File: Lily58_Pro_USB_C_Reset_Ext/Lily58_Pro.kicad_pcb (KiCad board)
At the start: 2 copper layers, 7.7 x 45.5 mm, 11 parts, among them J2 4PIN, P1 i2c_pin, P2 i2c_pin, U1 USB4110-GF-A_REVB, U2 USB4110-GF-A_REVB

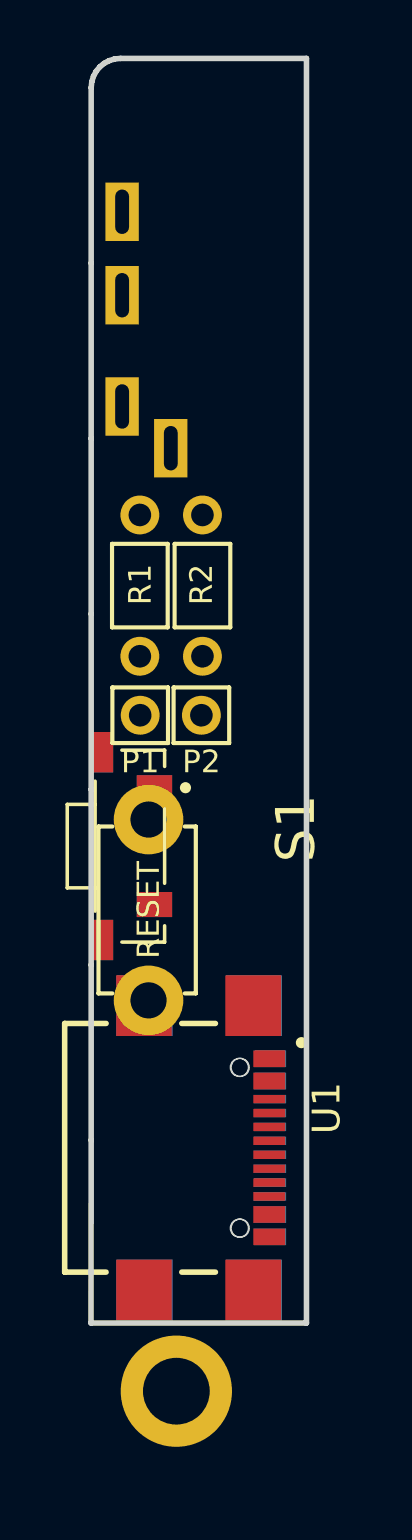
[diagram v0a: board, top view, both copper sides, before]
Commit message: Lily58_Pro_USB_C_Reset_Ext: routing
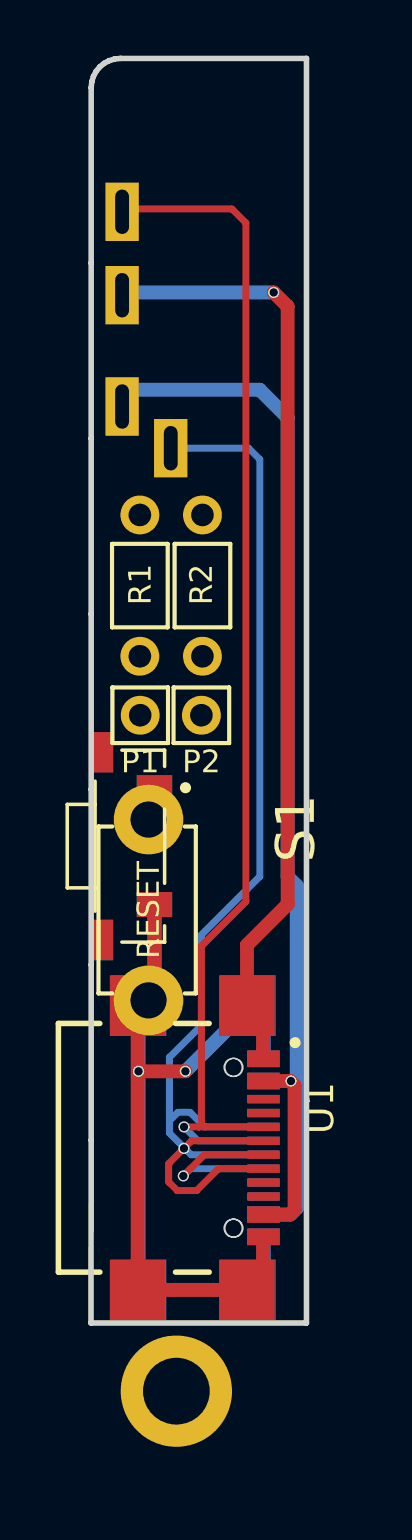
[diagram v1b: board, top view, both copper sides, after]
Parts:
- moved U2 0.23 mm to (88.1, 76.2)
- moved U1 0.22 mm to (88.0, 76.2)
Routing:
- net GND: track 0.00 -> 80.9 mm, vias 0 -> 3
- net SCL: track 0.00 -> 50.0 mm, vias 0 -> 2
- net VCC: track 0.00 -> 44.7 mm, vias 0 -> 1
- net SDA: track 0.00 -> 44.6 mm, vias 0 -> 1
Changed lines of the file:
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@@
   )
   (footprint "Usb:GCT_USB4110-GF-A_REVB" (layer "F.Cu")
-    (at 88.265 76.25 -90)
+    (at 88.04 76.25 -90)
     (property "MANUFACTURER" "GCT")
     (property "MAXIMUM_PACKAGE_HEIGHT" "3.26 mm")
@@
       (effects (font (size 1.4 1.4) (thickness 0.15)))
     )
-    (fp_text value "TL3330AF130QG" (at 9.194 -3.429 -90) (layer "F.Fab")
+    (fp_text value "TL3330AF130QG" (at 9.194 -3.204 -90) (layer "F.Fab")
       (effects (font (size 1.4 1.4) (thickness 0.15)))
     )
@@
   )
   (footprint "Usb:GCT_USB4110-GF-A_REVB" (layer "B.Cu")
-    (at 88.2955 76.25 90)
+    (at 88.0705 76.25 90)
     (property "MANUFACTURER" "GCT")
     (property "MAXIMUM_PACKAGE_HEIGHT" "3.26 mm")
@@
     (style (thickness 0.15) (arrow_length 1.27) (text_position_mode 0) (extension_height 0.58642) (extension_offset 0.5) keep_text_aligned)
   )
+  (segment (start 90.25 78.49) (end 90.09 78.65) (width 0.5) (layer "F.Cu") (net 1))
+  (segment (start 90.09 78.65) (end 89.115 78.65) (width 0.5) (layer "F.Cu") (net 1))
+  (segment (start 90.09 73.85) (end 90.25 74.01) (width 0.5) (layer "F.Cu") (net 1))
+  (segment (start 90.25 74.01) (end 90.25 78.49) (width 0.5) (layer "F.Cu") (net 1))
+  (segment (start 89.115 73.85) (end 90.09 73.85) (width 0.5) (layer "F.Cu") (net 1))
+  (via (at 90.1205 73.85) (size 0.4) (drill 0.3) (layers "F.Cu" "B.Cu") (net 1))
+  (segment (start 90.1 78.65) (end 90.328 78.422) (width 0.5) (layer "B.Cu") (net 1))
+  (segment (start 90.328 78.422) (end 90.328 74.0575) (width 0.5) (layer "B.Cu") (net 1))
+  (segment (start 90 50) (end 89 49) (width 0.5) (layer "B.Cu") (net 1))
+  (segment (start 84.5 49) (end 84.05 49.45) (width 0.5) (layer "B.Cu") (net 1))
+  (segment (start 90.328 74.0575) (end 90.1205 73.85) (width 0.5) (layer "B.Cu") (net 1))
+  (segment (start 89.1455 78.65) (end 90.1 78.65) (width 0.5) (layer "B.Cu") (net 1))
+  (segment (start 84.05 49.45) (end 84.05 49.6) (width 0.5) (layer "B.Cu") (net 1))
+  (segment (start 90 66.5) (end 90 50) (width 0.5) (layer "B.Cu") (net 1))
+  (segment (start 90.328 74.0575) (end 90.328 66.828) (width 0.5) (layer "B.Cu") (net 1))
+  (segment (start 90.328 66.828) (end 90 66.5) (width 0.5) (layer "B.Cu") (net 1))
+  (segment (start 90.1205 73.85) (end 89.1455 73.85) (width 0.5) (layer "B.Cu") (net 1))
+  (segment (start 89 49) (end 84.5 49) (width 0.5) (layer "B.Cu") (net 1))
+  (segment (start 89.115 73.05) (end 89.115 71.715) (width 0.5) (layer "F.Cu") (net 2))
+  (segment (start 85.213 67.505) (end 85.213 70.737) (width 0.5) (layer "F.Cu") (net 2))
+  (segment (start 84.61 71.14) (end 84.61 81.36) (width 0.5) (layer "F.Cu") (net 2))
+  (segment (start 89.115 80.785) (end 88.54 81.36) (width 0.5) (layer "F.Cu") (net 2))
+  (segment (start 88.54 71.14) (end 88.54 68.96) (width 0.5) (layer "F.Cu") (net 2))
+  (segment (start 84.61 81.36) (end 88.54 81.36) (width 0.5) (layer "F.Cu") (net 2))
+  (segment (start 89.115 79.45) (end 89.115 80.785) (width 0.5) (layer "F.Cu") (net 2))
+  (segment (start 84.6405 73.5) (end 86.325 73.5) (width 0.5) (layer "F.Cu") (net 2))
+  (segment (start 89.115 71.715) (end 88.54 71.14) (width 0.5) (layer "F.Cu") (net 2))
+  (segment (start 88.54 68.96) (end 90 67.5) (width 0.5) (layer "F.Cu") (net 2))
+  (segment (start 85.213 70.737) (end 85 70.95) (width 0.5) (layer "F.Cu") (net 2))
+  (segment (start 90 67.5) (end 90 46) (width 0.5) (layer "F.Cu") (net 2))
+  (segment (start 90 46) (end 89.5 45.5) (width 0.5) (layer "F.Cu") (net 2))
+  (via (at 84.6405 73.5) (size 0.4) (drill 0.3) (layers "F.Cu" "B.Cu") (net 2))
+  (via (at 86.325 73.5) (size 0.4) (drill 0.3) (layers "F.Cu" "B.Cu") (net 2))
+  (via (at 89.5 45.5) (size 0.4) (drill 0.3) (layers "F.Cu" "B.Cu") (net 2))
+  (segment (start 84.6405 81.36) (end 84.6405 71.14) (width 0.5) (layer "B.Cu") (net 2))
+  (segment (start 85.213 67.505) (end 85.213 70.737) (width 0.5) (layer "B.Cu") (net 2))
+  (segment (start 89.1455 71.715) (end 88.5705 71.14) (width 0.5) (layer "B.Cu") (net 2))
+  (segment (start 88.5705 71.2545) (end 86.325 73.5) (width 0.5) (layer "B.Cu") (net 2))
+  (segment (start 84.6405 81.36) (end 88.5705 81.36) (width 0.5) (layer "B.Cu") (net 2))
+  (segment (start 84.15 45.5) (end 84.05 45.6) (width 0.5) (layer "B.Cu") (net 2))
+  (segment (start 89.1455 79.45) (end 89.1455 80.785) (width 0.5) (layer "B.Cu") (net 2))
+  (segment (start 89.1455 80.785) (end 88.5705 81.36) (width 0.5) (layer "B.Cu") (net 2))
+  (segment (start 89.5 45.5) (end 84.15 45.5) (width 0.5) (layer "B.Cu") (net 2))
+  (segment (start 85.213 70.737) (end 85 70.95) (width 0.5) (layer "B.Cu") (net 2))
+  (segment (start 88.5705 71.14) (end 88.5705 71.2545) (width 0.5) (layer "B.Cu") (net 2))
+  (segment (start 89.1455 73.05) (end 89.1455 71.715) (width 0.5) (layer "B.Cu") (net 2))
+  (segment (start 85.725 77.479963) (end 86.032537 77.7875) (width 0.25) (layer "F.Cu") (net 3))
+  (segment (start 86.032537 77.7875) (end 86.729963 77.7875) (width 0.25) (layer "F.Cu") (net 3))
+  (segment (start 86.545037 76) (end 85.725 76.820037) (width 0.25) (layer "F.Cu") (net 3))
+  (segment (start 89.115 76) (end 86.545037 76) (width 0.25) (layer "F.Cu") (net 3))
+  (segment (start 86.729963 77.7875) (end 87.517463 77) (width 0.25) (layer "F.Cu") (net 3))
+  (segment (start 87.517463 77) (end 89.115 77) (width 0.25) (layer "F.Cu") (net 3))
+  (segment (start 85.725 76.820037) (end 85.725 77.479963) (width 0.25) (layer "F.Cu") (net 3))
+  (via (at 86.272519 76.272519) (size 0.4) (drill 0.3) (layers "F.Cu" "B.Cu") (net 3))
+  (segment (start 86.492463 74.975) (end 87.017463 75.5) (width 0.25) (layer "B.Cu") (net 3))
+  (segment (start 85.75 75.282537) (end 85.75 73) (width 0.25) (layer "B.Cu") (net 3))
+  (segment (start 88.6 51.1) (end 85.8 51.1) (width 0.25) (layer "B.Cu") (net 3))
+  (segment (start 85.75 75.282537) (end 86.057537 74.975) (width 0.25) (layer "B.Cu") (net 3))
+  (segment (start 85.75 73) (end 86.9 71.85) (width 0.25) (layer "B.Cu") (net 3))
+  (segment (start 87.017463 75.5) (end 89.1455 75.5) (width 0.25) (layer "B.Cu") (net 3))
+  (segment (start 89 66.5) (end 89 51.5) (width 0.25) (layer "B.Cu") (net 3))
+  (segment (start 86.9 68.6) (end 89 66.5) (width 0.25) (layer "B.Cu") (net 3))
+  (segment (start 85.75 75.717463) (end 85.75 75.282537) (width 0.25) (layer "B.Cu") (net 3))
+  (segment (start 86.532537 76.5) (end 85.75 75.717463) (width 0.25) (layer "B.Cu") (net 3))
+  (segment (start 89.1455 76.5) (end 86.532537 76.5) (width 0.25) (layer "B.Cu") (net 3))
+  (segment (start 86.057537 74.975) (end 86.492463 74.975) (width 0.25) (layer "B.Cu") (net 3))
+  (segment (start 86.9 71.85) (end 86.9 68.6) (width 0.25) (layer "B.Cu") (net 3))
+  (segment (start 89 51.5) (end 88.6 51.1) (width 0.25) (layer "B.Cu") (net 3))
+  (segment (start 84.15 42.5) (end 84.05 42.6) (width 0.25) (layer "F.Cu") (net 4))
+  (segment (start 86.8 75.5) (end 89.115 75.5) (width 0.25) (layer "F.Cu") (net 4))
+  (segment (start 88.5 43) (end 88 42.5) (width 0.25) (layer "F.Cu") (net 4))
+  (segment (start 86.25 77.2625) (end 87.0125 76.5) (width 0.25) (layer "F.Cu") (net 4))
+  (segment (start 87.0125 76.5) (end 89.115 76.5) (width 0.25) (layer "F.Cu") (net 4))
+  (segment (start 88 42.5) (end 84.15 42.5) (width 0.25) (layer "F.Cu") (net 4))
+  (segment (start 88.5 67.4) (end 88.5 43) (width 0.25) (layer "F.Cu") (net 4))
+  (segment (start 86.275 75.5) (end 86.8 75.5) (width 0.25) (layer "F.Cu") (net 4))
+  (segment (start 86.9 69) (end 88.5 67.4) (width 0.25) (layer "F.Cu") (net 4))
+  (segment (start 86.8 75.5) (end 86.9 75.4) (width 0.25) (layer "F.Cu") (net 4))
+  (segment (start 86.9 75.4) (end 86.9 69) (width 0.25) (layer "F.Cu") (net 4))
+  (via (at 86.275 75.5) (size 0.4) (drill 0.3) (layers "F.Cu" "B.Cu") (net 4))
+  (via (at 86.25 77.2625) (size 0.4) (drill 0.3) (layers "F.Cu" "B.Cu") (net 4))
+  (segment (start 86.5125 77) (end 89.1455 77) (width 0.25) (layer "B.Cu") (net 4))
+  (segment (start 86.275 75.5) (end 86.775 76) (width 0.25) (layer "B.Cu") (net 4))
+  (segment (start 86.775 76) (end 89.1455 76) (width 0.25) (layer "B.Cu") (net 4))
+  (segment (start 86.25 77.2625) (end 86.5125 77) (width 0.25) (layer "B.Cu") (net 4))
 )

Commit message: Lily58_Pro_USB_C_Reset_Ext: better routing
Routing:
- net SCL: track 50.0 -> 54.1 mm
- net GND: track 80.9 -> 83.6 mm, vias 3 -> 4
- net SDA: track 44.6 -> 42.4 mm, vias 1 -> 2
- added copper zone on B.Cu, net GND
- added copper zone on F.Cu, net GND
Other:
- board size 7.7 x 45.5 mm -> 7.7 x 47.2 mm

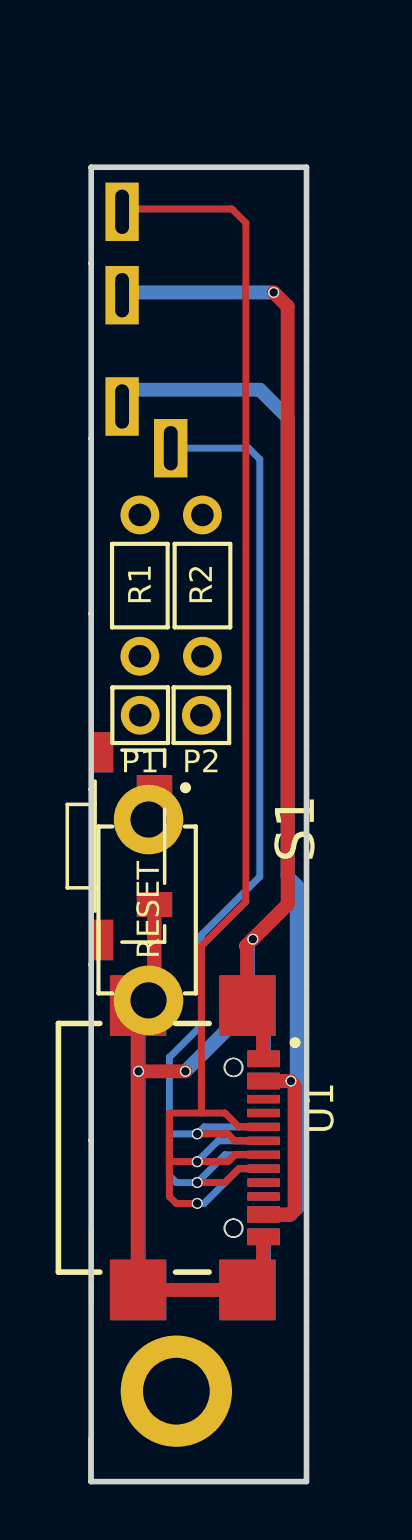
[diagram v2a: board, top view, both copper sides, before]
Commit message: Lily58_Pro_USB_C_Reset_Ext: remove fill
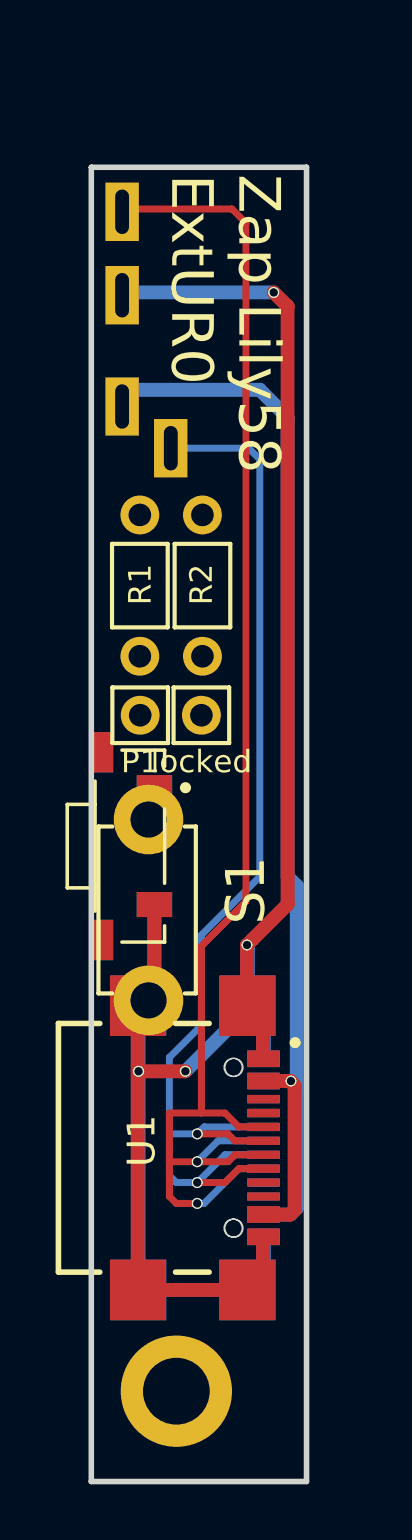
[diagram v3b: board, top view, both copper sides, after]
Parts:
- renumbered P2 to locked
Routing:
- removed copper zone on B.Cu, net GND
- removed copper zone on F.Cu, net GND
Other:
- outline, holes or cut-outs redrawn
- board text added: "Zap Lily58 ${TITLE}${REVISION}"
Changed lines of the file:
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@@
   )
   (paper "A4")
+  (title_block
+    (title "ExtUR")
+    (rev "0")
+  )
   (layers
     (0 "F.Cu" signal)
@@
     (autoplace_cost180 10)
     (attr through_hole)
-    (fp_text reference "P2" (at 0 -1.671944 180) (layer "F.SilkS")
+    (fp_text reference locked "P2" (at 0 -1.671944 180) (layer "F.SilkS")
       (effects (font (size 0.8128 0.8128) (thickness 0.15)))
     )
@@
     (fp_text value "SW_RST" (at 0 2 90) (layer "F.Fab") hide
       (effects (font (size 1 1) (thickness 0.15)))
-    )
-    (fp_text user "RESET" (at 0 0 270) (layer "B.SilkS")
-      (effects (font (size 0.8 0.8) (thickness 0.15)) (justify mirror))
-    )
-    (fp_text user "RESET" (at 0 0 90) (layer "F.SilkS")
-      (effects (font (size 0.8 0.8) (thickness 0.15)))
     )
     (fp_line (start 3 1.7) (end 3 1.3) (layer "B.SilkS") (width 0.15))
@@
     (property "Sheetname" "")
     (attr through_hole)
-    (fp_text reference "U1" (at -1.425 -3.135 -90) (layer "F.SilkS")
+    (fp_text reference "U1" (at -0.25 3.29 -90) (layer "F.SilkS")
       (effects (font (size 1 1) (thickness 0.15)))
     )
@@
     (property "Sheetname" "")
     (attr through_hole)
-    (fp_text reference "S1" (at -0.635 -5.969 -90) (layer "F.SilkS")
+    (fp_text reference "S1" (at 1.595 -4.172 -90) (layer "F.SilkS")
       (effects (font (size 1.4 1.4) (thickness 0.15)))
     )
@@
     (property "Sheetname" "")
     (attr through_hole)
-    (fp_text reference "U2" (at -1.425 3.135 270) (layer "B.SilkS")
+    (fp_text reference "U2" (at 0 -3.3205 270) (layer "B.SilkS")
       (effects (font (size 1 1) (thickness 0.15)) (justify mirror))
     )
@@
     (property "Sheetname" "")
     (attr through_hole)
-    (fp_text reference "S2" (at -0.635 5.969 270) (layer "B.SilkS")
+    (fp_text reference "S2" (at -1.595 4.172 270) (layer "B.SilkS")
       (effects (font (size 1.4 1.4) (thickness 0.15)) (justify mirror))
     )
@@
   )
   (gr_line (start 45.503294 -44.952764) (end 45.503294 -44.952764) (layer "Eco2.User") (width 0.1))
-  (gr_line (start 90.678 88.25) (end 82.931 88.25) (layer "Edge.Cuts") (width 0.2))
-  (gr_line (start 90.678 41) (end 90.678 88.25) (layer "Edge.Cuts") (width 0.2))
-  (gr_line (start 82.931 88.25) (end 82.937528 75.978362) (layer "Edge.Cuts") (width 0.2))
-  (gr_line (start 82.937528 50.750629) (end 82.937528 44.443695) (layer "Edge.Cuts") (width 0.2))
-  (gr_line (start 90.678 41) (end 82.93821 41) (layer "Edge.Cuts") (width 0.2))
-  (gr_line (start 82.937528 63.364495) (end 82.937528 57.057562) (layer "Edge.Cuts") (width 0.2))
-  (gr_line (start 82.937528 69.671429) (end 82.937528 63.364495) (layer "Edge.Cuts") (width 0.2))
-  (gr_line (start 82.937528 44.443695) (end 82.93821 41) (layer "Edge.Cuts") (width 0.2))
-  (gr_line (start 82.937528 75.978362) (end 82.937528 69.671429) (layer "Edge.Cuts") (width 0.2))
-  (gr_line (start 82.937528 57.057562) (end 82.937528 50.750629) (layer "Edge.Cuts") (width 0.2))
+  (gr_rect locked (start 82.942498 41.000086) (end 90.680136 88.247479) (layer "Edge.Cuts") (width 0.2) (fill none))
+  (gr_text "Zap Lily58\n${TITLE}${REVISION}" (at 87.75 41.25 270) (layer "B.SilkS")
+    (effects (font (size 1.5 1.5) (thickness 0.3)) (justify right mirror))
+  )
+  (gr_text "Zap Lily58\n${TITLE}${REVISION}" (at 87.75 41.25 270) (layer "F.SilkS")
+    (effects (font (size 1.5 1.5) (thickness 0.3)) (justify left))
+  )
   (dimension (type aligned) (layer "Dwgs.User")
     (pts (xy 90.678 88.25) (xy 90.678 41))
@@
   (segment (start 88.75 68.75) (end 90 67.5) (width 0.5) (layer "F.Cu") (net 2))
   (segment (start 90 67.5) (end 90 46) (width 0.5) (layer "F.Cu") (net 2))
-  (segment (start 89.115 73.05) (end 89.115 71.715) (width 0.5) (layer "F.Cu") (net 2))
   (segment (start 85.213 67.505) (end 85.213 70.737) (width 0.5) (layer "F.Cu") (net 2))
   (segment (start 84.61 71.14) (end 84.61 81.36) (width 0.5) (layer "F.Cu") (net 2))
@@
   (segment (start 89.115 79.45) (end 89.115 80.785) (width 0.5) (layer "F.Cu") (net 2))
   (segment (start 84.6405 73.5) (end 86.325 73.5) (width 0.5) (layer "F.Cu") (net 2))
-  (segment (start 89.115 71.715) (end 88.54 71.14) (width 0.5) (layer "F.Cu") (net 2))
   (segment (start 90 46) (end 89.5 45.5) (width 0.5) (layer "F.Cu") (net 2))
+  (segment (start 89.115 73.05) (end 89.115 71.715) (width 0.5) (layer "F.Cu") (net 2))
   (segment (start 85.213 70.737) (end 85 70.95) (width 0.5) (layer "F.Cu") (net 2))
   (segment (start 88.54 68.96) (end 88.75 68.75) (width 0.5) (layer "F.Cu") (net 2))
-  (segment (start 88.86 71.14) (end 88.54 71.14) (width 0.5) (layer "F.Cu") (net 2))
-  (segment (start 89 71) (end 88.86 71.14) (width 0.5) (layer "F.Cu") (net 2))
+  (segment (start 89.115 71.715) (end 88.54 71.14) (width 0.5) (layer "F.Cu") (net 2))
   (via (at 84.6405 73.5) (size 0.4) (drill 0.3) (layers "F.Cu" "B.Cu") (net 2))
   (via (at 86.325 73.5) (size 0.4) (drill 0.3) (layers "F.Cu" "B.Cu") (net 2))
+  (via (at 88.54 68.96) (size 0.4) (drill 0.3) (layers "F.Cu" "B.Cu") (net 2))
   (via (at 89.5 45.5) (size 0.4) (drill 0.3) (layers "F.Cu" "B.Cu") (net 2))
-  (via (at 88.75 68.75) (size 0.4) (drill 0.3) (layers "F.Cu" "B.Cu") (net 2))
   (segment (start 84.6405 81.36) (end 84.6405 71.14) (width 0.5) (layer "B.Cu") (net 2))
   (segment (start 85.213 67.505) (end 85.213 70.737) (width 0.5) (layer "B.Cu") (net 2))
+  (segment (start 88.5705 68.9905) (end 88.54 68.96) (width 0.5) (layer "B.Cu") (net 2))
   (segment (start 89.1455 71.715) (end 88.5705 71.14) (width 0.5) (layer "B.Cu") (net 2))
   (segment (start 88.5705 71.2545) (end 86.325 73.5) (width 0.5) (layer "B.Cu") (net 2))
   (segment (start 84.6405 81.36) (end 88.5705 81.36) (width 0.5) (layer "B.Cu") (net 2))
   (segment (start 84.15 45.5) (end 84.05 45.6) (width 0.5) (layer "B.Cu") (net 2))
+  (segment (start 88.5705 71.14) (end 88.5705 68.9905) (width 0.5) (layer "B.Cu") (net 2))
   (segment (start 89.1455 79.45) (end 89.1455 80.785) (width 0.5) (layer "B.Cu") (net 2))
   (segment (start 89.1455 80.785) (end 88.5705 81.36) (width 0.5) (layer "B.Cu") (net 2))
   (segment (start 89.5 45.5) (end 84.15 45.5) (width 0.5) (layer "B.Cu") (net 2))
-  (segment (start 88.5705 71.14) (end 88.5705 69.0705) (width 0.5) (layer "B.Cu") (net 2))
   (segment (start 85.213 70.737) (end 85 70.95) (width 0.5) (layer "B.Cu") (net 2))
   (segment (start 88.5705 71.14) (end 88.5705 71.2545) (width 0.5) (layer "B.Cu") (net 2))
   (segment (start 89.1455 73.05) (end 89.1455 71.715) (width 0.5) (layer "B.Cu") (net 2))
-  (segment (start 88.5705 69.0705) (end 88.5 69) (width 0.5) (layer "B.Cu") (net 2))
   (segment (start 87.853604 75.75) (end 86.75 75.75) (width 0.25) (layer "F.Cu") (net 3))
   (segment (start 88.25 77) (end 87.75 77.5) (width 0.25) (layer "F.Cu") (net 3))
@@
   (segment (start 86.75 78.25) (end 87 78.25) (width 0.25) (layer "B.Cu") (net 4))
   (segment (start 86.75 76.75) (end 87.5 76) (width 0.25) (layer "B.Cu") (net 4))
-  (zone (net 2) (net_name "GND") (layer "F.Cu") (hatch edge 0.508)
-    (connect_pads (clearance 0.508))
-    (min_thickness 0.254) (filled_areas_thickness no)
-    (fill yes (thermal_gap 0.508) (thermal_bridge_width 0.508))
-    (polygon
-      (pts
-        (xy 90.75 88.25)
-        (xy 83 88.25)
-        (xy 83 41)
-        (xy 90.75 41)
-      )
-    )
-  )
-  (zone (net 2) (net_name "GND") (layer "B.Cu") (hatch edge 0.508)
-    (connect_pads (clearance 0.508))
-    (min_thickness 0.254) (filled_areas_thickness no)
-    (fill yes (thermal_gap 0.508) (thermal_bridge_width 0.508))
-    (polygon
-      (pts
-        (xy 90.75 88.25)
-        (xy 83 88.25)
-        (xy 83 41)
-        (xy 90.75 41)
-      )
-    )
-  )
 )
